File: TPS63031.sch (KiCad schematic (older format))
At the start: 10 parts, among them J1 Conn_01x03, J2 Conn_01x03, U1 TPS63031

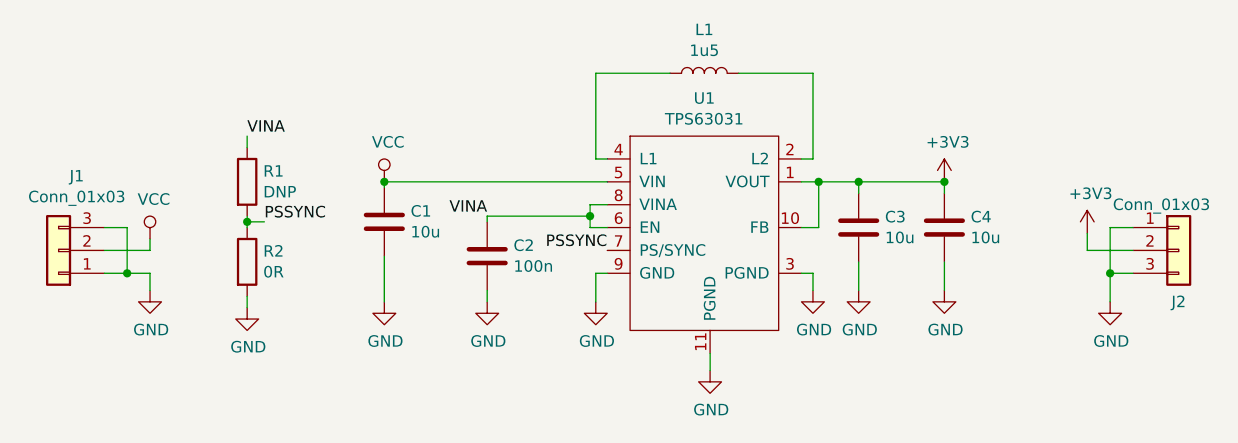
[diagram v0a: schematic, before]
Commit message: Inductor type specification
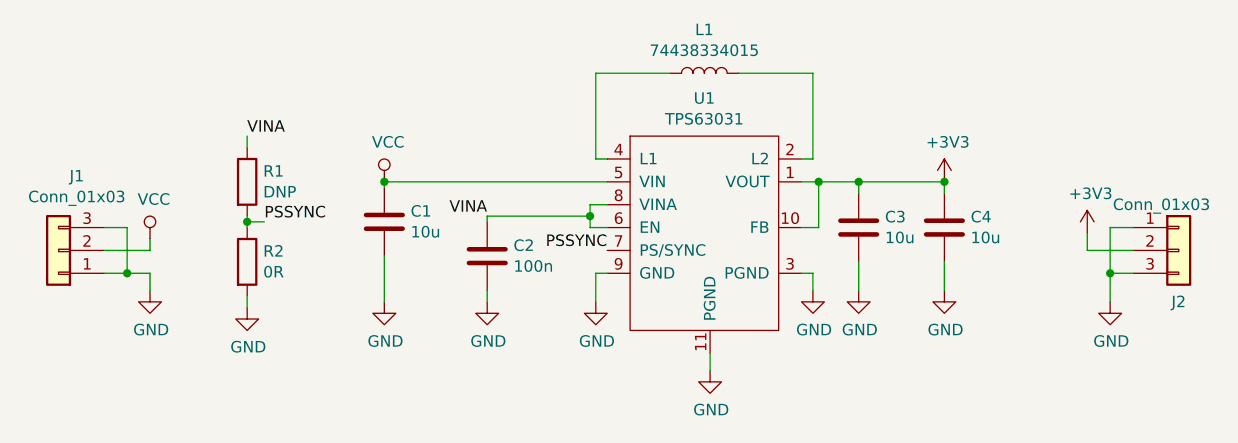
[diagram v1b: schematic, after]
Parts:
- L1: value 1u5 -> 74438334015
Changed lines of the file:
@@
 EESchema Schematic File Version 4
+LIBS:TPS63031-cache
 EELAYER 26 0
 EELAYER END
@@
 P 5650 2925
 F 0 "L1" V 5840 2925 50  0000 C CNN
-F 1 "1u5" V 5749 2925 50  0000 C CNN
+F 1 "74438334015" V 5749 2925 50  0000 C CNN
 F 2 "Inductor_SMD:L_Wuerth_MAPI-3012" H 5650 2925 50  0001 C CNN
 F 3 "" H 5650 2925 50  0001 C CNN

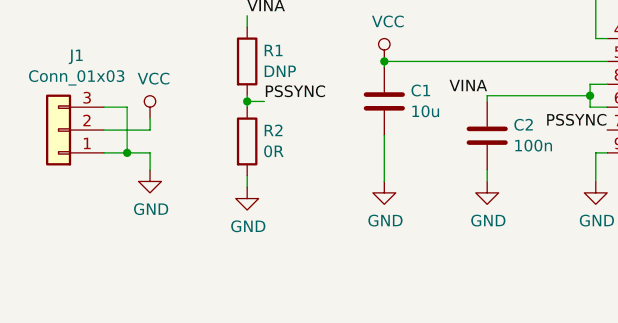
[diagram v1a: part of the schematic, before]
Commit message: Added description how to set converter mode
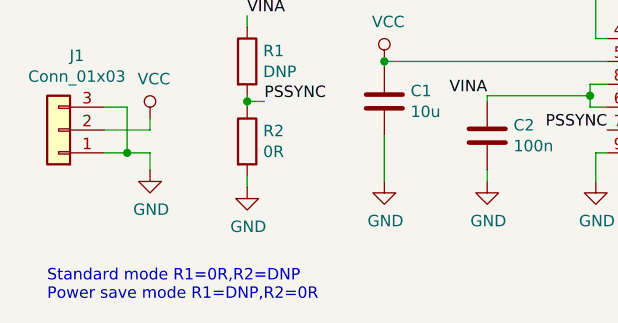
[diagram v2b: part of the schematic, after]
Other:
- note added: "Standard mode R1=0R,R2=DNP\nPower save mode R1=DNP,R2=0R"
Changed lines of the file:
@@
 EESchema Schematic File Version 4
 LIBS:TPS63031-cache
-EELAYER 26 0
+EELAYER 29 0
 EELAYER END
 $Descr A4 11693 8268
@@
 Text Label 3650 3200 0    50   ~ 0
 VINA
+Text Notes 2775 4450 0    50   ~ 0
+Standard mode R1=0R,R2=DNP\nPower save mode R1=DNP,R2=0R
 $EndSCHEMATC
